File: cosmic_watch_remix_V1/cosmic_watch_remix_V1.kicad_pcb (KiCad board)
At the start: 2 copper layers, 87.6 x 94.6 mm, 10 parts, among them IC1 MICROFJ-60035-TSV-TR1, J1 Conn_01x05_Female, U1 ADS1115IDGS

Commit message: Component Initial Layout Complete
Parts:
- added C2: C, Capacitor_SMD:C_0603_1608Metric, F.Cu at (116.0, 100.0)
- added C3: C, Capacitor_SMD:C_0603_1608Metric, F.Cu at (120.5, 100.0)
- added C4: 1uF, Capacitor_SMD:C_0603_1608Metric, F.Cu at (68.5, 36.6)
- added C5: 50pF, Capacitor_SMD:C_0603_1608Metric, F.Cu at (70.0, 24.9)
- added C6: 1uF, Capacitor_SMD:C_0603_1608Metric, F.Cu at (64.6, 29.5)
- added C7: 0.47pF, Capacitor_SMD:C_0603_1608Metric, F.Cu at (63.1, 29.5)
- added C8: 1uF, Capacitor_SMD:C_0603_1608Metric, F.Cu at (58.6, 29.5)
- added C9: ?, Capacitor_SMD:C_0603_1608Metric, F.Cu at (76.8, 133.0)
- added D1: DIODE, Diode_SMD:D_SOD-323, F.Cu at (71.5, 123.8)
- added D2: DIODE, Diode_SMD:D_SOD-323, F.Cu at (74.2, 132.2)
- added IC2: LT3461AES6#TRMPBF, Package_TO_SOT_SMD:TSOT-23-6, F.Cu at (68.5, 30.4)
- added L1: L_Ferrite, Resistor_SMD:R_0603_1608Metric, F.Cu at (118.2, 99.2)
- added L2: 18uH, Inductor_SMD:L_1210_3225Metric, F.Cu at (68.5, 34.0)
- added L3: 2.5k Ferrite, Resistor_SMD:R_0603_1608Metric, F.Cu at (60.8, 30.2)
- added R10: ?, Resistor_SMD:R_0603_1608Metric, F.Cu at (87.8, 71.5)
- added R5: 10K, Resistor_SMD:R_0603_1608Metric, F.Cu at (72.0, 29.0)
- added R6: 280K, Resistor_SMD:R_0603_1608Metric, F.Cu at (70.0, 26.4)
- added R7: 10K, Resistor_SMD:R_0603_1608Metric, F.Cu at (68.0, 28.0)
- added R8: 10K, Resistor_SMD:R_0603_1608Metric, F.Cu at (65.8, 128.8)
- added R9: 10K, Resistor_SMD:R_0603_1608Metric, F.Cu at (76.5, 124.0)
- added U2: LM358, Package_SO:SOIC-8_7.5x5.85mm_P1.27mm, F.Cu at (74.0, 128.0)
- moved R2 60.5 mm to (87.5, 68.1), turned to 90 degrees
- moved R4 52.5 mm to (97.5, 68.7), turned to -90 degrees
- moved C1 49.3 mm to (96.0, 71.2), turned to -90 degrees
- moved R1 47.3 mm to (85.7, 68.8), turned to -90 degrees
- moved U1 46.4 mm to (91.4, 70.1)
- moved R3 42.7 mm to (96.0, 67.9), turned to -90 degrees
- moved IC1 0.27 mm to (53.0, 91.4)
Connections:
- IC1 pad A1: unconnected-(IC1-PadA1) -> VBIAS
- IC1 pad A2: unconnected-(IC1-PadA2) -> GND
- IC1 pad A3: unconnected-(IC1-PadA3) -> GND
- IC1 pad A4: unconnected-(IC1-PadA4) -> GND
- IC1 pad A5: unconnected-(IC1-PadA5) -> GND
- IC1 pad A6: unconnected-(IC1-PadA6) -> GND
- IC1 pad B1: unconnected-(IC1-PadB1) -> GND
- IC1 pad B2: unconnected-(IC1-PadB2) -> GND
- IC1 pad B3: unconnected-(IC1-PadB3) -> GND
- IC1 pad B4: unconnected-(IC1-PadB4) -> GND
- IC1 pad B5: unconnected-(IC1-PadB5) -> GND
- IC1 pad B6: unconnected-(IC1-PadB6) -> GND
- IC1 pad C1: unconnected-(IC1-PadC1) -> Net-(IC1-PadC1)
- IC1 pad C2: unconnected-(IC1-PadC2) -> GND
- IC1 pad C3: unconnected-(IC1-PadC3) -> GND
- IC1 pad C4: unconnected-(IC1-PadC4) -> GND
- IC1 pad C5: unconnected-(IC1-PadC5) -> GND
- IC1 pad D1: unconnected-(IC1-PadD1) -> Net-(IC1-PadC1)
- IC1 pad D2: unconnected-(IC1-PadD2) -> GND
- IC1 pad D3: unconnected-(IC1-PadD3) -> GND
- IC1 pad D4: unconnected-(IC1-PadD4) -> GND
- IC1 pad D5: unconnected-(IC1-PadD5) -> GND
- IC1 pad E1: unconnected-(IC1-PadE1) -> GND
- IC1 pad E2: unconnected-(IC1-PadE2) -> GND
- IC1 pad E3: unconnected-(IC1-PadE3) -> GND
- IC1 pad E4: unconnected-(IC1-PadE4) -> GND
- IC1 pad E5: unconnected-(IC1-PadE5) -> GND
- IC1 pad E6: unconnected-(IC1-PadE6) -> GND
- IC1 pad F1: unconnected-(IC1-PadF1) -> GND
- IC1 pad F2: unconnected-(IC1-PadF2) -> GND
- IC1 pad F3: unconnected-(IC1-PadF3) -> GND
- IC1 pad F4: unconnected-(IC1-PadF4) -> GND
- IC1 pad F5: unconnected-(IC1-PadF5) -> GND
- IC1 pad F6: unconnected-(IC1-PadF6) -> VBIAS
- U1 pad 4: unconnected-(U1-Pad4) -> Net-(U1-Pad4)
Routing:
- net GND: track 0.00 -> 14.9 mm, vias 0 -> 12
- net Net-(D1-Pad1): track 0.00 -> 14.0 mm
- net Net-(D1-Pad2): track 0.00 -> 11.3 mm
- net Net-(U1-Pad4): track 0.00 -> 7.21 mm
- net Net-(C5-Pad2): track 0.00 -> 5.27 mm
- net Net-(C9-Pad1): track 0.00 -> 5.00 mm
- net /VIN: track 0.00 -> 4.56 mm
- net VDDA: track 0.00 -> 3.92 mm
- net Net-(J1-Pad4): track 0.00 -> 3.91 mm
- net Net-(J1-Pad2): track 0.00 -> 3.59 mm
- net /VOUT: track 0.00 -> 3.09 mm
- net Net-(J1-Pad3): track 0.00 -> 2.53 mm
- net Net-(R8-Pad2): track 0.00 -> 2.15 mm
- net Net-(R2-Pad1): track 0.00 -> 1.83 mm
- net Net-(IC2-Pad4): track 0.00 -> 1.54 mm
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- added copper zone on F.Cu, net /VIN
- added copper zone on F.Cu, net /VOUT
- added copper zone on B.Cu, net GND
- added copper zone on F.Cu, net GND
- added copper zone on F.Cu, net Net-(C5-Pad2)
- added copper zone on F.Cu, net VDDA
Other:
- board text added: "ADS1115 Analog to Digital Converter"
- board text added: "DC-DC Boost"
- board text added: "Peak Detector"

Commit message: V1.0
Finished Layout, Ready to Review!
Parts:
- removed the ? at (103.4, 137.1)
- removed the ? at (23.4, 137.1)
- removed C2, C3: C, Capacitor_SMD:C_0603_1608Metric
- removed L1: L_Ferrite, Resistor_SMD:R_0603_1608Metric
- added ?: , , F.Cu at (36.0, 122.0)
- added ?: , , F.Cu at (92.0, 66.0)
- added ?: , , F.Cu at (92.0, 122.0)
- added ?: , , F.Cu at (36.0, 66.0)
- added G***: LOGO, LOGO, B.Cu at (64.0, 94.0)
- U2: footprint Package_SO:SOIC-8_7.5x5.85mm_P1.27mm -> Package_SO:SOIC-8-1EP_3.9x4.9mm_P1.27mm_EP2.29x3mm
- moved J1 71.7 mm to (27.0, 94.0), turned to -90 degrees
- moved R4 71.3 mm to (26.2, 71.3), turned to 0 degrees
- moved R3 70.7 mm to (25.4, 72.8), turned to 0 degrees
- moved C1 67.3 mm to (28.6, 72.8), turned to 0 degrees
- moved U1 64.2 mm to (27.6, 77.3), turned to 90 degrees
- moved R2 63.4 mm to (25.6, 81.2), turned to 180 degrees
- moved R1 61.9 mm to (24.1, 74.3), turned to 180 degrees
- moved R10 59.5 mm to (29.0, 81.0), turned to 180 degrees
- moved D2 56.7 mm to (25.3, 103.6)
- moved C9 56.4 mm to (28.7, 103.6), turned to 0 degrees
- moved R9 55.7 mm to (23.5, 106.8), turned to 90 degrees
- moved U2 50.7 mm to (27.0, 109.0), turned to 90 degrees
- moved D1 50.0 mm to (23.2, 110.8), turned to -90 degrees
- moved C5 48.0 mm to (36.6, 59.4), turned to 180 degrees
- moved R6 45.9 mm to (36.6, 57.9), turned to 0 degrees
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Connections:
- C1 pad 1: VDDA -> VCC
- C4 pad 1: VDDA -> VCC
- IC2 pad 1: VDDA -> VCC
- L2 pad 1: VDDA -> VCC
- U1 pad 3: GNDA -> GND
- U1 pad 8: VDDA -> VCC
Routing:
- net VBIAS: track 1.47 -> 90.1 mm
- net VCC: track 1.44 -> 56.3 mm, vias 0 -> 2
- net Net-(IC1-PadC1): track 0.00 -> 43.4 mm
- net Net-(R10-Pad2): track 7.21 -> 32.8 mm
- net Net-(J1-Pad4): track 3.91 -> 27.6 mm
- net Net-(J1-Pad3): track 2.53 -> 24.6 mm
- net Net-(J1-Pad2): track 3.59 -> 21.9 mm, vias 0 -> 2
- net Net-(D1-Pad1): track 14.0 -> 9.72 mm
- net VDDA: track 3.92 -> 0.00 mm
- net GND: track 14.9 -> 16.7 mm, vias 12 -> 14
- net Net-(D1-Pad2): track 11.3 -> 12.6 mm
- net /VIN: track 4.56 -> 3.57 mm
- added copper zone on B.Cu, net (none)
- added copper zone on F.Cu, net (none)
- added copper zone on F.Cu, net VCC
- removed copper zone on F.Cu, net VDDA
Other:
- outline, holes or cut-outs redrawn
- board text added: "Cosmic Watch Remix V1.0 Made By: Michael Pham Cosmic Watch Team: Luke Kohler, Michael Quach, Matt Roberts For the Pleiades - Squared Mission January 2023"

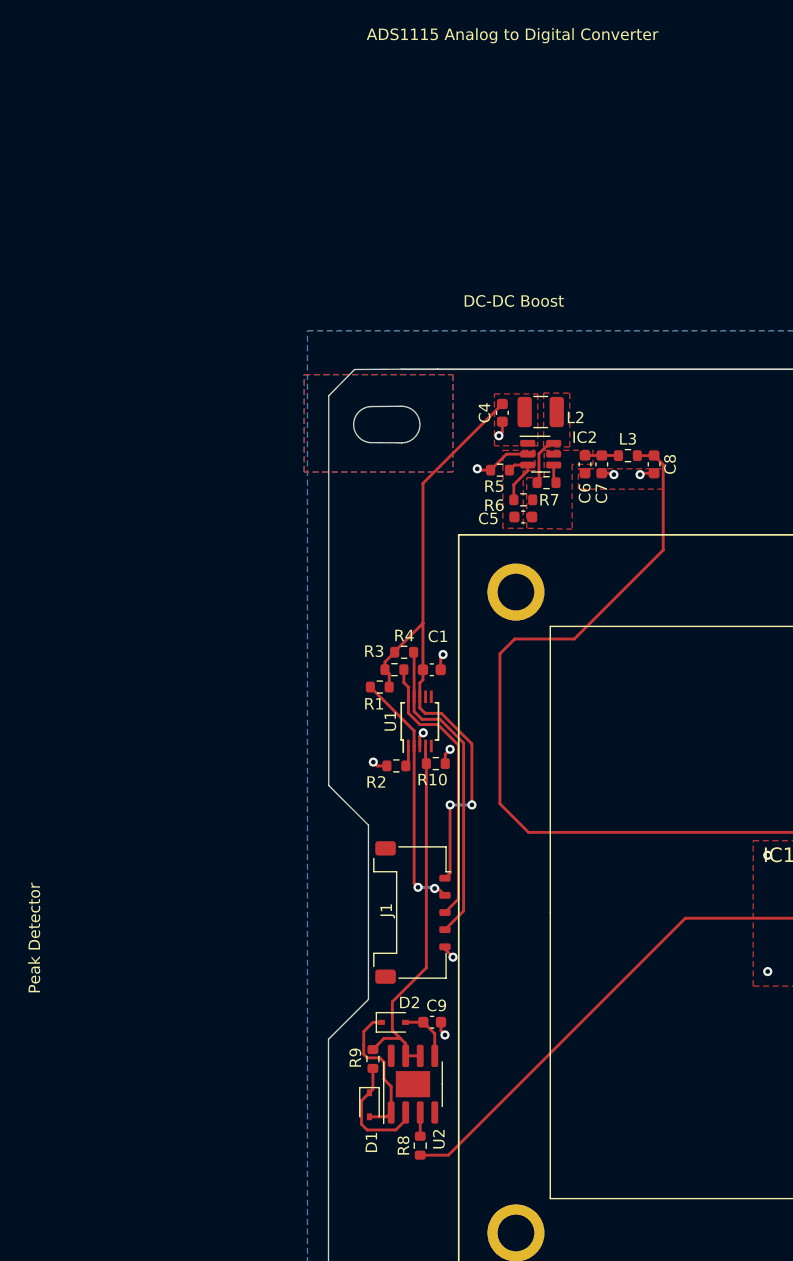
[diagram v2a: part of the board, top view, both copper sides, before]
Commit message: Completed Component Selection
Note change to 28V output
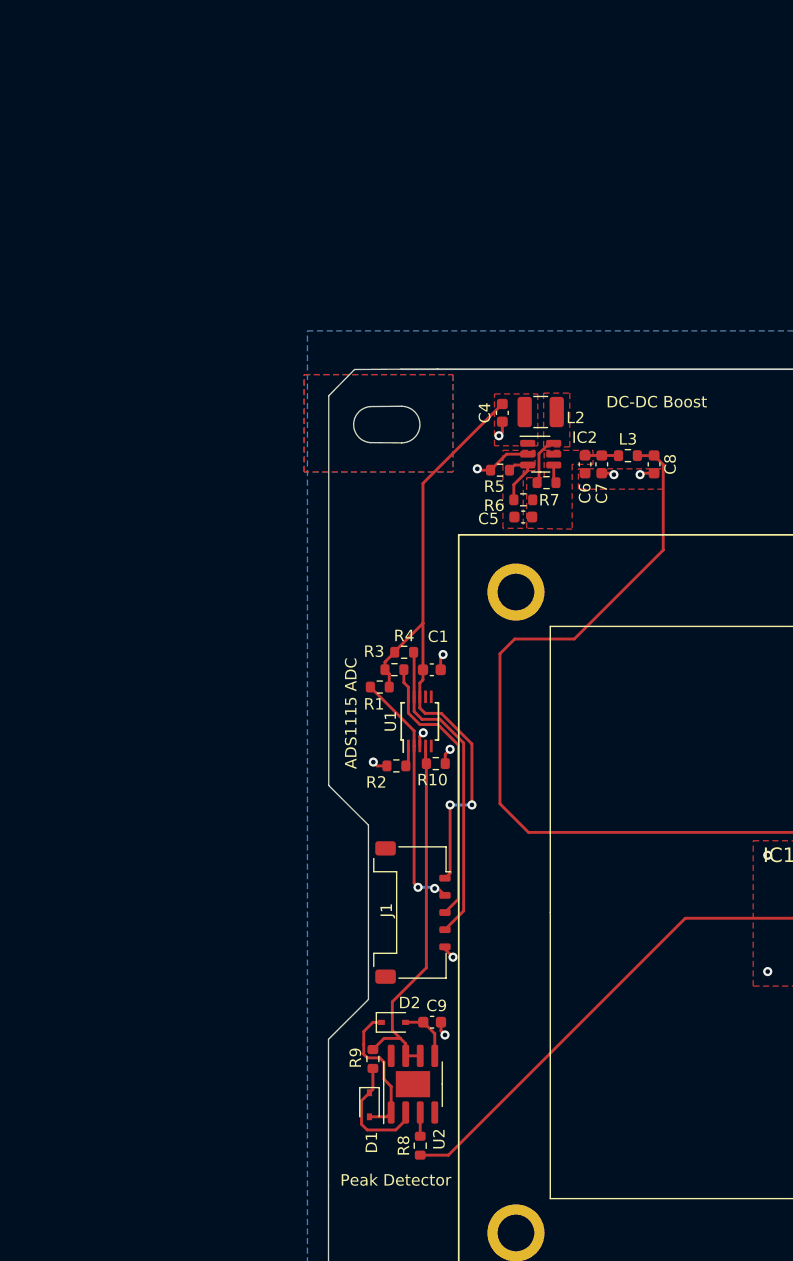
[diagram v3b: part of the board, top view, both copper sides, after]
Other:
- board text added: "ADS1115 ADC"
- board text removed: "ADS1115 Analog to Digital Converter"
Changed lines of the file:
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@@
   (gr_arc locked (start 102.17 122.09) (mid 101.271974 121.718026) (end 100.9 120.82) (layer "Edge.Cuts") (width 0.15))
   (gr_line (start 19.64 48.85) (end 19.64 82.9) (layer "Edge.Cuts") (width 0.1))
-  (gr_text "DC-DC Boost" (at 35.8 40.6) (layer "F.SilkS")
+  (gr_text "DC-DC Boost" (at 48.3 49.4) (layer "F.SilkS")
     (effects (font (size 1 1) (thickness 0.15)))
   )
-  (gr_text "Peak Detector" (at -6.05 96.25 90) (layer "F.SilkS")
+  (gr_text "Peak Detector" (at 25.5 117.4) (layer "F.SilkS")
     (effects (font (size 1 1) (thickness 0.15)))
   )
-  (gr_text "ADS1115 Analog to Digital Converter" (at 35.7 17.3) (layer "F.SilkS")
+  (gr_text "ADS1115 ADC\n" (at 21.6 76.6 90) (layer "F.SilkS")
     (effects (font (size 1 1) (thickness 0.15)))
   )
